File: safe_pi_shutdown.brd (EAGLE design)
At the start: 42.4 x 27 mm, 33 parts, among them IC1 MCP73831, IC2 LTC2952CF, IC3 MT3608, Q1 IRF7342, Q2 IRF7342, X1 MICRO-USB-RECEPTACLE47589-0001, X4 MF-CON-2.54mm-01x02, X5 MF-CON-2.54mm-01x02

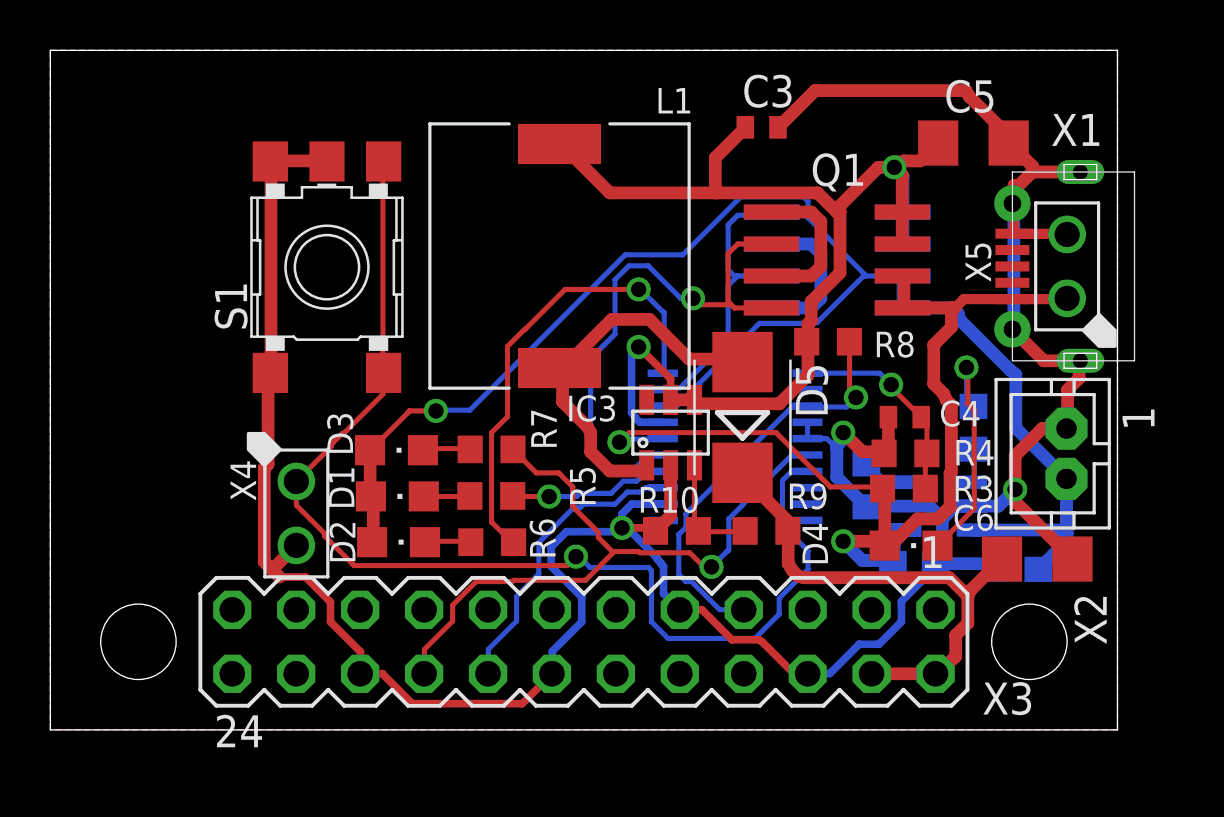
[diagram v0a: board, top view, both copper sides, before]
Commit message: dodanie pull-up dla pinu INT
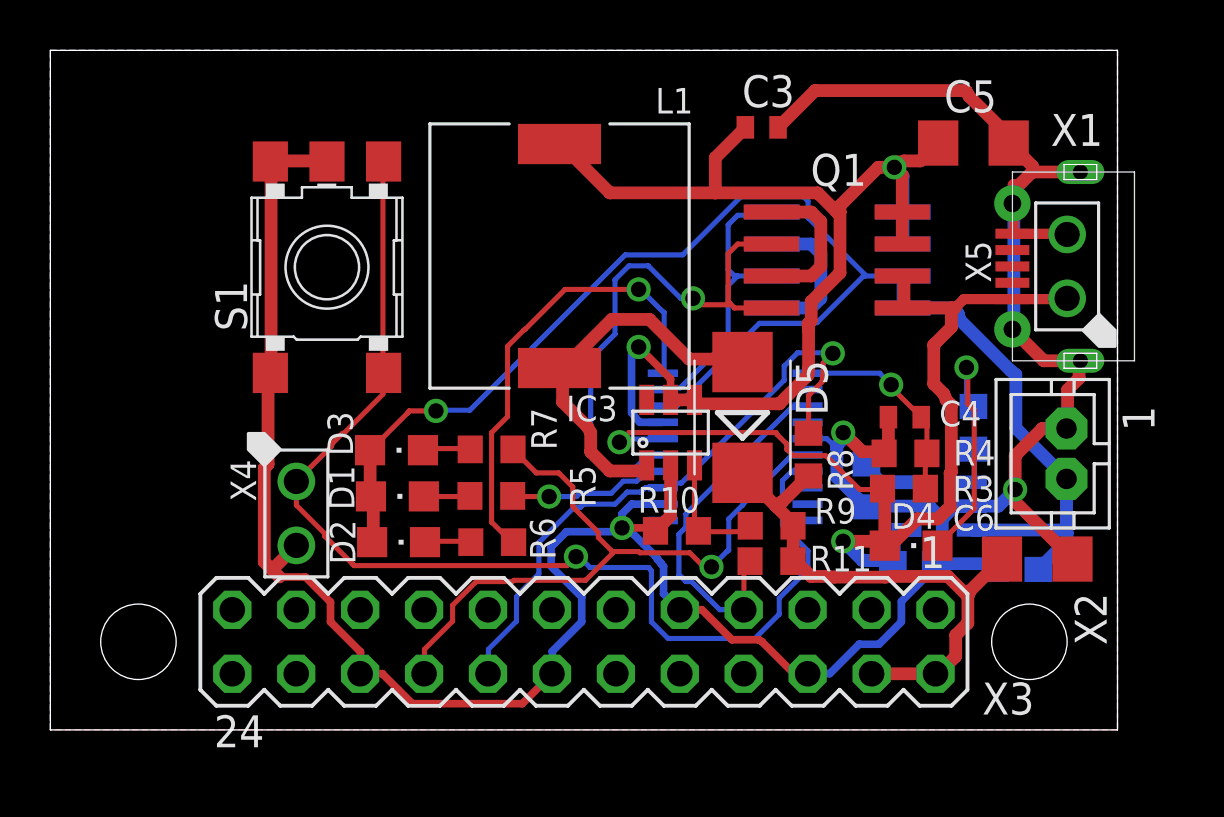
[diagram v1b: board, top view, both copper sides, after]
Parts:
- added R11: 10k, rcl:R0603
- C5: value 10u -> 22u
- moved R8 4.55 mm to (30.1, 10.9), turned to 90 degrees
- moved R9 0.29 mm to (28.7, 8.11)
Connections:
- net N$10: now also R8.2
- net N$12: now also R11.1; no longer R8.2
- net N$4: now also R11.2, R8.1
- net VCC: no longer R8.1
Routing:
- net N$10: track 11.9 -> 25.0 mm, vias 0 -> 1
- net N$12: track 16.7 -> 14.3 mm, vias 1 -> 0
- net N$4: track 20.3 -> 21.9 mm

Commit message: boost converter changed to MIC2876
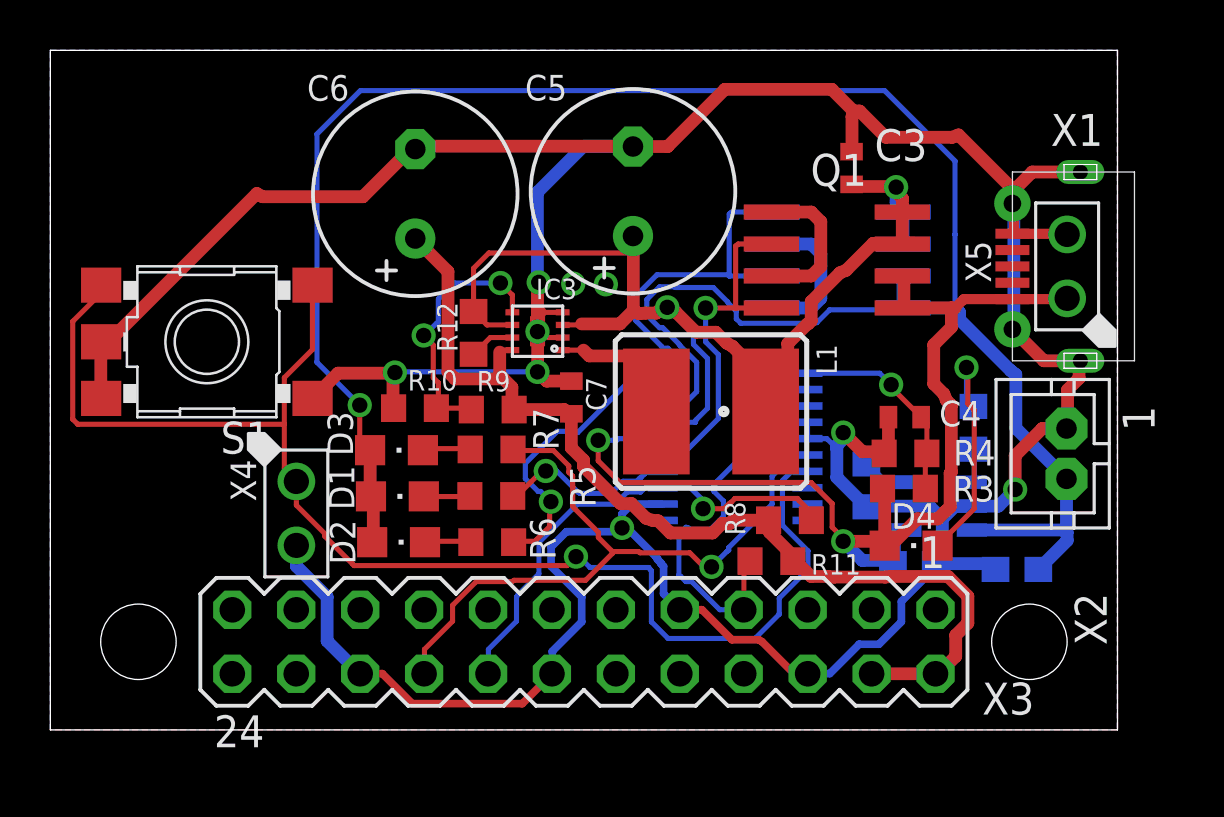
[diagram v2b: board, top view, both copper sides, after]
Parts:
- removed D5: (no value), eagle-ltspice:DIODE_SMB
- added C7: 100n, rcl:C0402
- added R12: 910k, rcl:R0603
- C5, C6: value 22u -> 220u; device rcl:C1206 -> rcl:E3,5-8
- IC3: value MT3608 -> MIC2876; device mt3608:SOT23-6 -> mic2876:MIC2876
- L1: value 2.2u -> 1u; device SparkFun-Passives:DR1030 -> SparkFun-Passives:CR54-KIT
- moved C6 28.7 mm to (14.5, 21.3), turned to 90 degrees
- moved C5 13.7 mm to (23.1, 21.4), turned to 90 degrees
- moved R9 12.0 mm to (17.6, 12.7)
- moved R10 11.5 mm to (14.5, 12.8)
- moved L1 8.63 mm to (26.2, 12.7), turned to 270 degrees
- moved IC3 6.65 mm to (19.4, 15.8), turned to 90 degrees
- moved S1 5.62 mm to (6.22, 15.4), turned to 180 degrees
- moved C3 3.92 mm to (31.8, 22.3), turned to 270 degrees
- moved R8 2.71 mm to (29.4, 8.33), turned to 0 degrees
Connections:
- removed net N$13: D5.A, IC3.1, L1.2
- removed net N$21: IC3.3, R10.1, R9.2
- new net N$11: IC3.P$7, R12.2
- new net N$7: IC3.P$5, R10.1, R9.2
- new net N$9: IC3.P$1, L1.P$2
- net GND: now also C5.-, C6.-, C7.2, IC3.P$2, IC3.P$4; no longer C5.2, C6.2, IC3.2
- net N$4: now also C6.+, C7.1, IC3.P$8; no longer C6.1, D5.C
- net VCC: now also C5.+, IC3.P$3, IC3.P$6, L1.P$1, R12.1; no longer C5.1, IC3.4, IC3.5, L1.1
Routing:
- net GND: track 128.5 -> 160.7 mm, vias 3 -> 9
- net V1: track 61.0 -> 87.9 mm
- net N$4: track 21.9 -> 40.5 mm
- net N$13: track 16.3 -> 0.00 mm
- net N$7: track 0.00 -> 10.8 mm, vias 0 -> 2
- net N$5: track 45.8 -> 54.4 mm
- net N$3: track 21.6 -> 13.9 mm
- net N$19: track 18.4 -> 11.7 mm
- net N$10: track 25.0 -> 19.2 mm
- net N$9: track 0.00 -> 5.70 mm
- net N$21: track 4.83 -> 0.00 mm
- net N$2: track 11.7 -> 15.5 mm
- net N$11: track 0.00 -> 1.82 mm
- net V2: track 41.4 -> 43.0 mm
- net N$12: track 14.3 -> 15.3 mm
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
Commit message: add more capacitors to power path
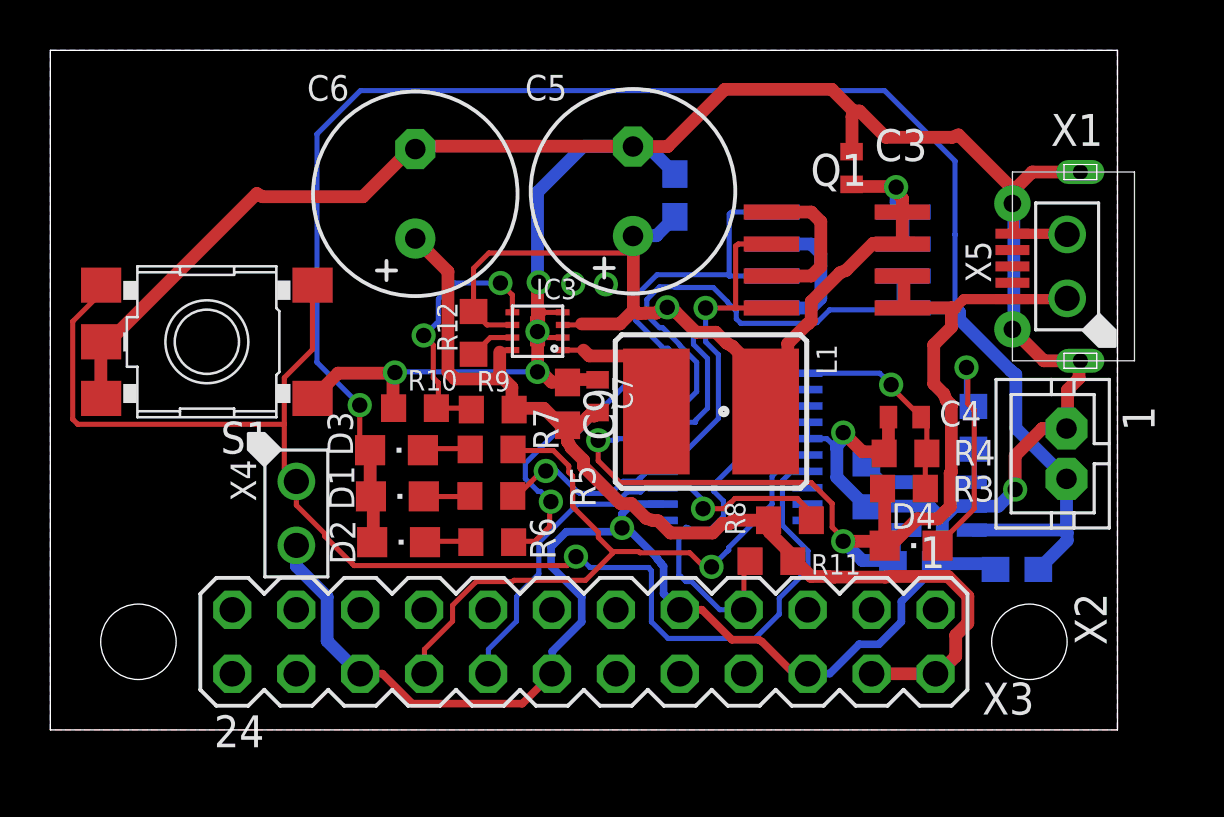
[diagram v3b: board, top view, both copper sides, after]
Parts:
- added C8, C9: 22u, rcl:C0603
- moved C7 1.04 mm to (21.7, 13.3)
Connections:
- net GND: now also C8.2, C9.1
- net N$4: now also C9.2
- net VCC: now also C8.1
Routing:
- net GND: track 160.7 -> 163.9 mm
- net VCC: track 48.1 -> 50.1 mm
- net N$4: track 40.5 -> 41.8 mm
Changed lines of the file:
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@@
 <?xml version="1.0" encoding="utf-8"?>
 <!DOCTYPE eagle SYSTEM "eagle.dtd">
-<eagle version="6.5.0">
+<eagle version="6.6.0">
 <drawing>
 <settings>
@@
 <attribute name="VALUE" x="17.548" y="19.014" size="1.27" layer="27" ratio="10" rot="R90"/>
 </element>
-<element name="C7" library="rcl" package="C0402" value="100n" x="20.701" y="13.208" smashed="yes" rot="R90">
-<attribute name="NAME" x="22.098" y="12.6746" size="0.8128" layer="25" font="vector" rot="R90"/>
-<attribute name="VALUE" x="22.606" y="12.573" size="1.27" layer="27" rot="R90"/>
-</element>
+<element name="C7" library="rcl" package="C0402" value="100n" x="21.7424" y="13.2588" smashed="yes" rot="R90">
+<attribute name="NAME" x="23.1394" y="12.7254" size="0.8128" layer="25" font="vector" rot="R90"/>
+<attribute name="VALUE" x="23.6474" y="12.6238" size="1.27" layer="27" rot="R90"/>
+</element>
+<element name="C8" library="rcl" package="C0603" value="22u" x="24.8158" y="21.2344" rot="MR90"/>
+<element name="C9" library="rcl" package="C0603" value="22u" x="20.5486" y="12.954" rot="R270"/>
 </elements>
 <signals>
@@
 <wire x1="13.6144" y1="13.9192" x2="13.6906" y2="14.1986" width="0.508" layer="1"/>
 <wire x1="13.6144" y1="12.8016" x2="13.6378" y2="12.78335" width="0.508" layer="1"/>
-<wire x1="20.701" y1="13.858" x2="19.7208" y2="13.858" width="0.508" layer="1"/>
-<wire x1="19.7208" y1="13.858" x2="19.3548" y2="14.224" width="0.508" layer="1"/>
 <wire x1="20.3578" y1="16.5896" x2="19.4598" y2="16.5896" width="0.2032" layer="1"/>
 <wire x1="19.3548" y1="16.4846" x2="19.3548" y2="15.8242" width="0.2032" layer="1"/>
@@
 <wire x1="19.4598" y1="16.5896" x2="19.3836" y2="16.5896" width="0.508" layer="1"/>
 <wire x1="19.3836" y1="16.5896" x2="19.3548" y2="16.5608" width="0.508" layer="1"/>
+<contactref element="C8" pad="2"/>
+<contactref element="C9" pad="1"/>
+<wire x1="23.7236" y1="23.1902" x2="23.368" y2="23.1902" width="0.508" layer="16"/>
+<wire x1="24.8158" y1="22.098" x2="23.7236" y2="23.1902" width="0.508" layer="16"/>
+<wire x1="23.368" y1="23.1902" x2="23.15" y2="23.178" width="0.508" layer="16"/>
+<wire x1="24.8158" y1="22.098" x2="24.8158" y2="22.0844" width="0.508" layer="16"/>
+<wire x1="19.9136" y1="13.8176" x2="20.5486" y2="13.8176" width="0.508" layer="1"/>
+<wire x1="19.6088" y1="14.1224" x2="19.9136" y2="13.8176" width="0.508" layer="1"/>
+<wire x1="20.5486" y1="13.8176" x2="20.5486" y2="13.804" width="0.508" layer="1"/>
+<wire x1="19.6088" y1="14.1224" x2="19.3548" y2="14.224" width="0.508" layer="1"/>
+<wire x1="20.7772" y1="13.9192" x2="21.7424" y2="13.9192" width="0.508" layer="1"/>
+<wire x1="21.7424" y1="13.9192" x2="21.7424" y2="13.9088" width="0.508" layer="1"/>
+<wire x1="20.7772" y1="13.9192" x2="20.5486" y2="13.804" width="0.508" layer="1"/>
+<wire x1="19.3802" y1="17.7292" x2="19.4056" y2="17.78" width="0" layer="19" extent="1-1"/>
+<wire x1="20.7772" y1="17.7292" x2="20.3578" y2="16.5896" width="0" layer="19" extent="1-1"/>
+<wire x1="22.0726" y1="17.7038" x2="20.7772" y2="17.7292" width="0" layer="19" extent="1-1"/>
 </signal>
 <signal name="N$2">
@@
 <wire x1="33.7566" y1="20.8026" x2="33.87975" y2="20.574" width="0.508" layer="16"/>
 <via x="33.6042" y="21.5646" extent="1-16" drill="0.6096"/>
+<contactref element="C8" pad="1"/>
+<wire x1="24.0792" y1="19.6342" x2="23.1648" y2="19.6342" width="0.508" layer="16"/>
+<wire x1="24.8158" y1="20.3708" x2="24.0792" y2="19.6342" width="0.508" layer="16"/>
+<wire x1="23.1648" y1="19.6342" x2="23.15" y2="19.622" width="0.508" layer="16"/>
+<wire x1="24.8158" y1="20.3708" x2="24.8158" y2="20.3844" width="0.508" layer="16"/>
 </signal>
 <signal name="N$16">
@@
 <wire x1="28.2702" y1="8.3312" x2="28.5376" y2="8.3298" width="0.508" layer="1"/>
 <wire x1="24.1554" y1="8.3058" x2="23.9014" y2="8.3312" width="0.508" layer="1"/>
-<wire x1="18.4404" y1="12.7254" x2="18.4264" y2="12.72675" width="0.508" layer="1"/>
 <wire x1="18.3896" y1="12.9794" x2="18.4264" y2="12.72675" width="0.508" layer="1"/>
-<wire x1="20.701" y1="12.5476" x2="20.701" y2="12.558" width="0.508" layer="1"/>
-<wire x1="20.701" y1="11.2014" x2="20.701" y2="12.558" width="0.508" layer="1"/>
 <wire x1="21.1836" y1="10.7188" x2="20.701" y2="11.2014" width="0.508" layer="1"/>
 <wire x1="21.1836" y1="10.7188" x2="21.1836" y2="10.4648" width="0.508" layer="1"/>
-<wire x1="20.4216" y1="12.7254" x2="18.4404" y2="12.7254" width="0.508" layer="1"/>
-<wire x1="20.4724" y1="12.6746" x2="20.4216" y2="12.7254" width="0.508" layer="1"/>
-<wire x1="20.4724" y1="12.6746" x2="20.701" y2="12.558" width="0.508" layer="1"/>
 <contactref element="C6" pad="+"/>
 <wire x1="16.0782" y1="13.9446" x2="18.0086" y2="13.9446" width="0.508" layer="1"/>
@@
 <wire x1="17.8562" y1="15.0114" x2="17.8562" y2="14.097" width="0.508" layer="1"/>
 <wire x1="17.8562" y1="14.097" x2="18.0086" y2="13.9446" width="0.508" layer="1"/>
+<contactref element="C9" pad="2"/>
+<wire x1="20.5486" y1="11.4554" x2="20.5486" y2="12.104" width="0.508" layer="1"/>
+<wire x1="20.574" y1="11.43" x2="20.5486" y2="11.4554" width="0.508" layer="1"/>
+<wire x1="20.574" y1="11.43" x2="20.701" y2="11.2014" width="0.508" layer="1"/>
+<wire x1="21.3868" y1="12.4714" x2="20.7772" y2="11.8618" width="0.508" layer="1"/>
+<wire x1="21.6154" y1="12.4714" x2="21.3868" y2="12.4714" width="0.508" layer="1"/>
+<wire x1="21.7424" y1="12.5984" x2="21.6154" y2="12.4714" width="0.508" layer="1"/>
+<wire x1="20.7772" y1="11.8618" x2="20.5486" y2="12.104" width="0.508" layer="1"/>
+<wire x1="21.7424" y1="12.5984" x2="21.7424" y2="12.6088" width="0.508" layer="1"/>
+<wire x1="19.6088" y1="12.7762" x2="18.669" y2="12.7762" width="0.508" layer="1"/>
+<wire x1="20.2946" y1="12.0904" x2="19.6088" y2="12.7762" width="0.508" layer="1"/>
+<wire x1="18.669" y1="12.7762" x2="18.4264" y2="12.72675" width="0.508" layer="1"/>
+<wire x1="20.2946" y1="12.0904" x2="20.5486" y2="12.104" width="0.508" layer="1"/>
 </signal>
 <signal name="N$10">
